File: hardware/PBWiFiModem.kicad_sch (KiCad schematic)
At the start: 20 parts, among them J1 Conn_02x10_Odd_Even, J2 Conn_01x06_Pin, U1 LM1117MP-3.3, U2 TXS0108EPW, U3 ESP-12F

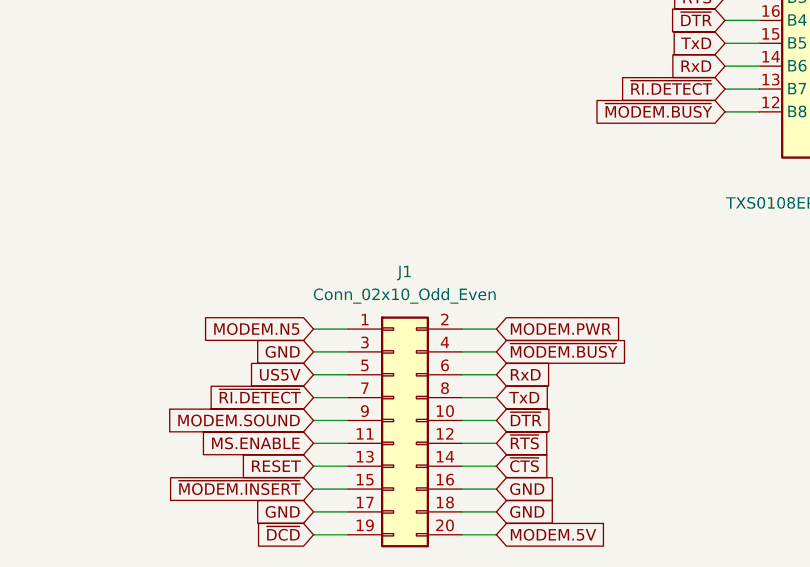
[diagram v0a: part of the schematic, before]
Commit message: Connector changed to SMD
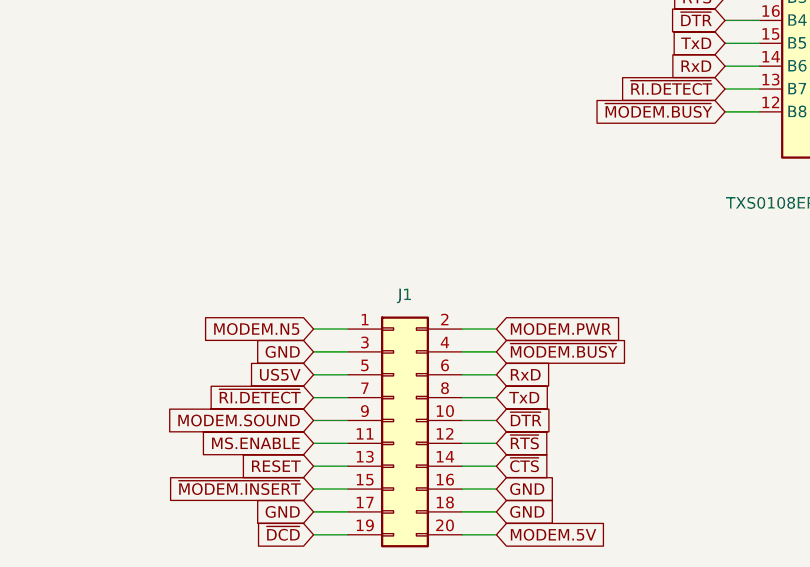
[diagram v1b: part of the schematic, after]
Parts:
- J1: footprint Connector_PinHeader_1.27mm:PinHeader_2x10_P1.27mm_Vertical -> Connector_PinSocket_1.27mm:PinSocket_2x10_P1.27mm_Vertical_SMD
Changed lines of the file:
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@@
   )
   (symbol (lib_id "Connector_Generic:Conn_02x10_Odd_Even") (at 66.04 91.44 0) (unit 1)
-    (in_bom yes) (on_board yes) (dnp no) (fields_autoplaced)
-    (property "Reference" "J1" (at 67.31 74.93 0)
+    (in_bom yes) (on_board yes) (dnp no)
+    (property "Reference" "J1" (at 67.31 77.47 0)
       (effects (font (size 1.27 1.27)))
     )
     (property "Value" "Conn_02x10_Odd_Even" (at 67.31 77.47 0)
-      (effects (font (size 1.27 1.27)))
-    )
-    (property "Footprint" "Connector_PinHeader_1.27mm:PinHeader_2x10_P1.27mm_Vertical" (at 66.04 91.44 0)
       (effects (font (size 1.27 1.27)) hide)
     )
+    (property "Footprint" "Connector_PinSocket_1.27mm:PinSocket_2x10_P1.27mm_Vertical_SMD" (at 66.04 91.44 0)
+      (effects (font (size 1.27 1.27)) hide)
+    )
